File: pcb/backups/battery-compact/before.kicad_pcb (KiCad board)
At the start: 2 copper layers, 115 parts, among them J1 B2B-PH-K-S, J3 B2B-PH-K-S, J4 104031-0811, Q1 AO3400A, Q2 AO3400A, SW1 PTS841GKSMTR LFS, SW2 JS202011AQN, U1 113991114, U10 SN74CBTLV3245APWR, U11 SN74CBTLV3245APWR, U3 MAX17048G+T10, U4 BMI270, U5 TPS61023DRLR, U6 AP2112K-3.3TRG1, U7 TPS22918DBVR, U8 TPS22918DBVR, U9 TPS22918DBVR

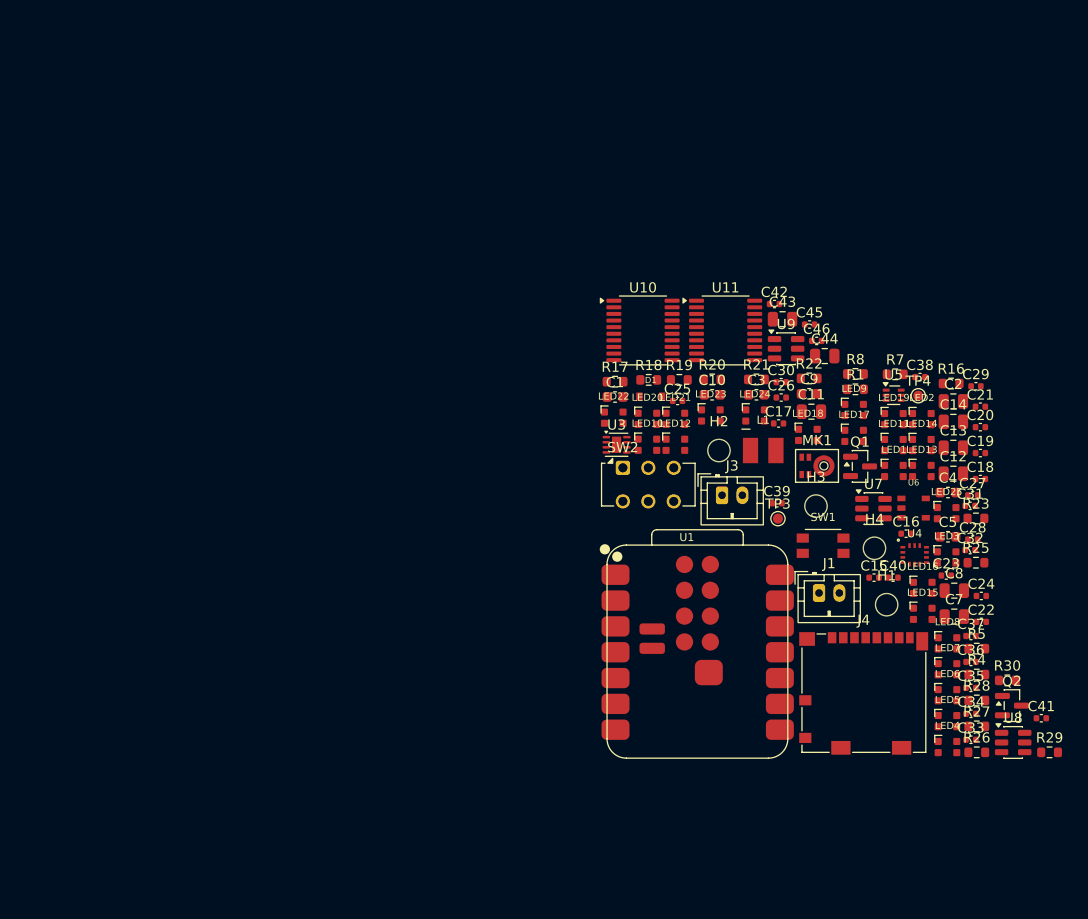
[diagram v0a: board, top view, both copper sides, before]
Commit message: Add compact placement candidate and update BOM, layout, and component library
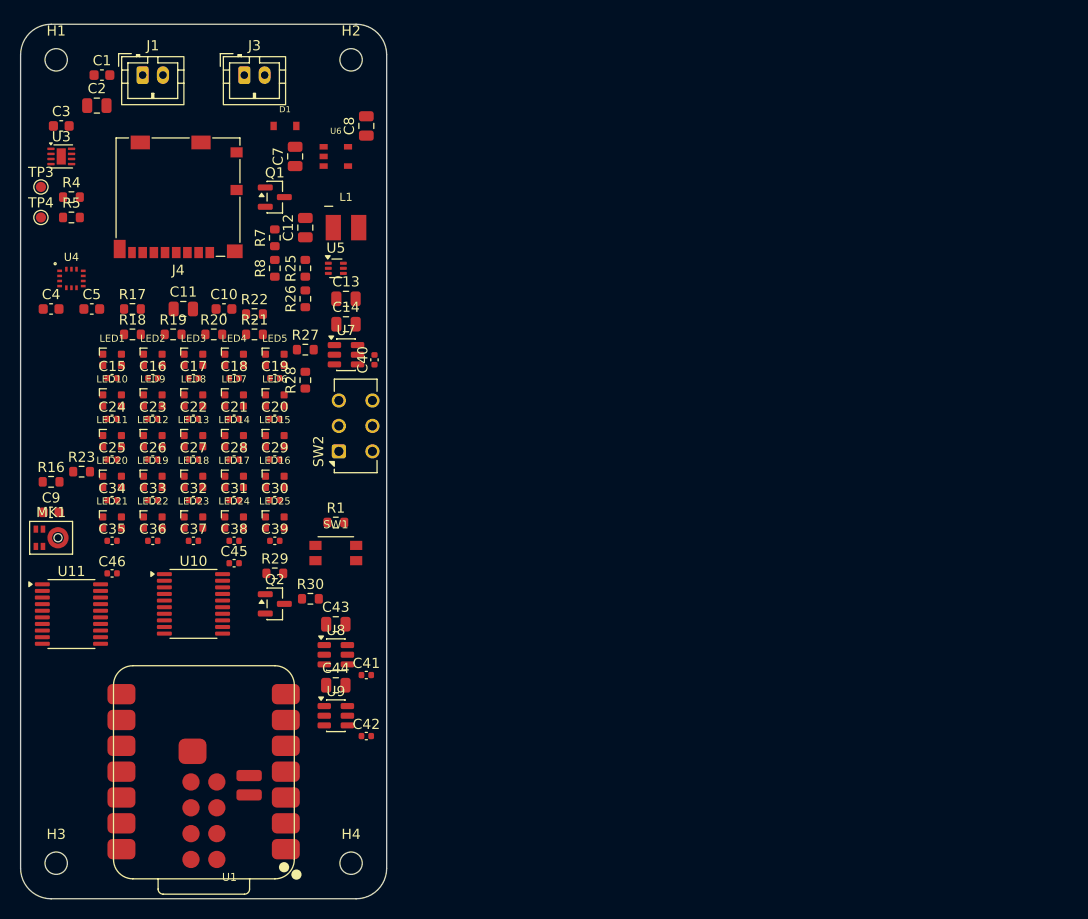
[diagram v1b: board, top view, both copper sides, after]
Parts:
- moved R4 100.7 mm to (87.0, 61.0)
- moved R5 98.6 mm to (87.0, 63.0)
- moved H1 97.7 mm to (85.5, 47.5)
- moved C4 90.0 mm to (85.0, 72.0)
- moved C2 89.1 mm to (89.5, 52.0)
- moved R16 89.0 mm to (85.0, 89.0)
- moved R23 88.1 mm to (88.0, 88.0)
- moved TP4 88.0 mm to (84.0, 63.0)
- moved U4 87.3 mm to (87.0, 69.0)
- moved C24 87.2 mm to (91.0, 82.8)
- moved C5 87.1 mm to (89.0, 72.0)
- moved C34 87.0 mm to (91.0, 90.8)
- moved C35 85.7 mm to (91.0, 94.8)
- moved C33 83.8 mm to (95.0, 90.8)
- moved J1 83.8 mm to (94.0, 49.0)
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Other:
- board outline added: 36 x 86 mm
